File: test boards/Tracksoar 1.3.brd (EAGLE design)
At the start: 50.4 x 19.5 mm, 46 parts, among them IC1 BME280, IC2 74AHC1G125DBV, Y1 16MHZ

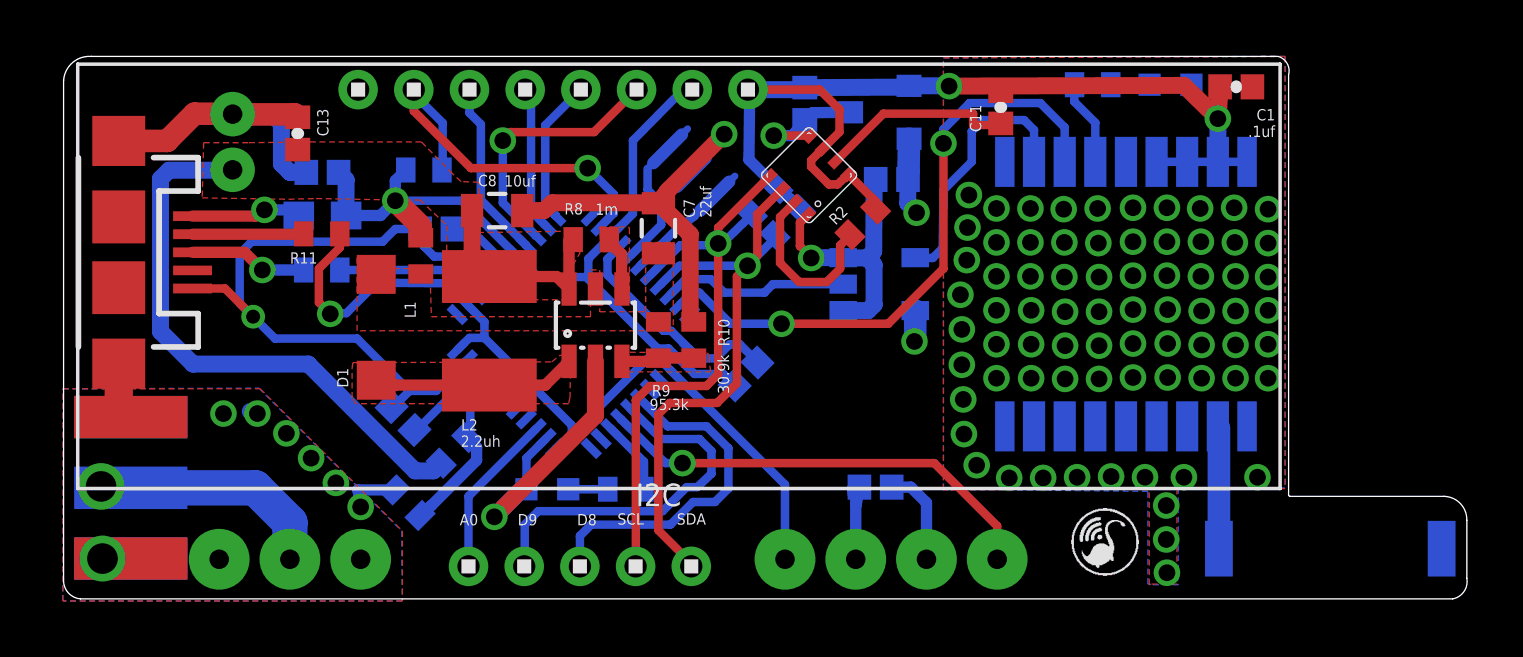
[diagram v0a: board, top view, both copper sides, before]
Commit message: Tracksoar V1.3
Created a new test board Tracksoar v1.3 to resolve potential issues
with the boost converter interfering with GPS reception.
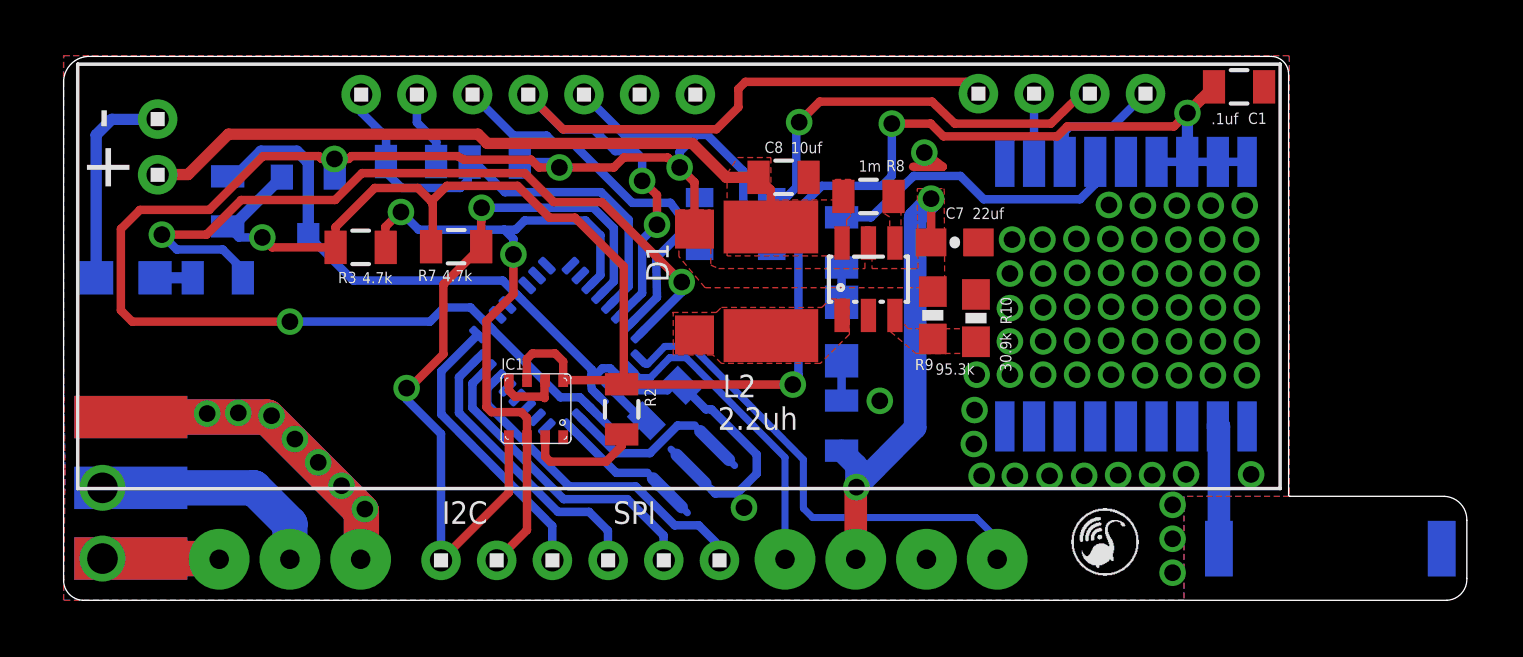
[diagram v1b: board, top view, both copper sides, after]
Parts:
- removed C10, C11, C13, C9: .1uf, SparkFun-Capacitors:0402-CAP
- removed C12: 1uf, SparkFun-Capacitors:0402-CAP
- removed C6: .1uf, SparkFun-Passives:0402-CAP
- removed F1: PTC0603, SparkFun-PowerIC:0603
- removed J1: (no value), SparkFun-Connectors:JST-2-PTH
- removed JP1: USB-MICROB, SparkFun-Connectors:USB-MICROB
- removed L1: BLM15HB121SN1, inductors:0402
- removed R11, R4: 22ohm, adafruit:R0402
- removed R13: 10k, adafruit:R0402
- removed U$4: ATMEGA32U4QFN2, SparkFun-DigitalIC:QFN-44-NOPAD
- added SERIAL: 1X4, headers(2mm):1X4
- added SPI/I2C: 1X6, headers(2mm):1X6
- added U1: ATMEGA328P, SparkFun-DigitalIC:MLF32
- C1, C2, C3, C4: device SparkFun-Capacitors:0402-CAP -> SparkFun-Capacitors:0805
- C5: value 1uf -> .1uf; device SparkFun-Capacitors:0402-CAP -> SparkFun-Capacitors:0805
- C7: device SparkFun-Capacitors:0805 -> SparkFun-Capacitors:0603-CAP
- FTDI: value 1X8 -> 1X7; device headers(2mm):1X8 -> headers(2mm):1X7
- GPSLOCK, PTT: device adafruit:CHIP-LED0603 -> adafruit:CHIP-LED0805
- R1, R2, R3, R5, R6, R7, R8: device adafruit:R0402 -> SparkFun-Resistors:0805
- R10, R9: device adafruit:R0402 -> SparkFun-Resistors:0603-RES
- U$3: value 1X5 -> 1X2; device headers(2mm):1X5 -> headers(2mm):1X2
- moved U$3 21.4 mm to (3.40, 16.3), turned to 90 degrees
- moved C2 21.0 mm to (5.92, 14.4), turned to 270 degrees
- moved LM3480 20.8 mm to (8.81, 14.2), turned to 180 degrees
- moved PTT 16.9 mm to (2.26, 11.6)
- moved R6 16.5 mm to (5.56, 11.6)
- moved R3 15.4 mm to (10.7, 12.7), flipped to the top, turned to 0 degrees
- moved GPSLOCK 14.8 mm to (28.0, 9.68), turned to 180 degrees
- moved IC1 12.9 mm to (17.0, 6.91), turned to 0 degrees
- moved D1 11.5 mm to (22.7, 11.5)
- moved C3 11.5 mm to (21.6, 7.11), turned to 315 degrees
- moved R7 11.2 mm to (14.1, 12.7), flipped to the top, turned to 0 degrees
- moved R2 11.0 mm to (20.1, 6.88), turned to 270 degrees
- moved Y1 10.7 mm to (22.6, 4.73), turned to 315 degrees
- moved C7 10.7 mm to (32.0, 12.9), turned to 0 degrees
- moved R1 10.6 mm to (28.0, 12.9), turned to 270 degrees
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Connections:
- removed net A0: U$3.1, U$4.36
- removed net D+: R4.2, U$4.4
- removed net D-: R11.2, U$4.3
- removed net D13: U$4.32
- removed net D8: U$3.3, U$4.28
- removed net D9: U$3.2, U$4.29
- removed net N$17: C12.2, U$4.42
- removed net N$19: C7.1, D1.C, L1.1, LT3426.5, R9.2
- removed net N$20: C5.2, U$4.6
- removed net N$7: JP1.D-, R11.1
- removed net N$8: JP1.D+, R4.1
- removed net RX: U$1.3_RXD1, U$4.21
- removed net VIN: C13.2, C8.1, J1.2, L2.1, LT3426.6, R13.1, R8.2
- removed net VSENSE: C6.2, R13.2, U$4.41
- removed net XTAL1: U$4.17, Y1.1
- removed net XTAL2: U$4.16, Y1.3
- new net 15V: C8.1, L2.1, LT3426.6, R8.2, U$3.1
- new net DTR: C5.1, FTDI.6
- new net N$26: U1.7, Y1.1
- new net RX1: SERIAL.1, U$1.3_RXD1
- new net RXO: FTDI.4, SERIAL.4, U1.30
- new net TXO: FTDI.5, IC2.2, U1.31
- net !RESET: now also C5.2, U1.29; no longer U$4.13
- net 3V: no longer C11.2, FTDI.1
- net D3: now also U1.1; no longer U$4.30
- net D4: now also U1.2; no longer U$4.25
- net GND: now also FTDI.1, FTDI.2, U$3.2, U1.21, U1.3, U1.5; no longer C10.1, C11.1, C12.1, C13.1, C5.1, C6.1, C9.1, FTDI.8, J1.1, JP1.GND, JP1.MT1, JP1.MT2, U$4.15, U$4.23, U$4.35, U$4.43, U$4.5
- net LED: now also U1.32; no longer U$4.31
- net MISO: now also SPI/I2C.4, U1.16; no longer FTDI.4, U$4.11
- net MOSI: now also SPI/I2C.5, U1.15; no longer FTDI.5, U$4.10
- net N$14: now also U1.8, Y1.3; no longer F1.1, JP1.VBUS
- net SCK: now also SPI/I2C.3, U1.17; no longer FTDI.3, U$4.9
- net SCL: now also SPI/I2C.1, U1.28; no longer U$3.4, U$4.18
- net SDA: now also SPI/I2C.2, U1.27; no longer U$3.5, U$4.19
- net SS: now also SPI/I2C.6, U1.14; no longer FTDI.6, U$4.8
- net TX: now also SERIAL.3, U$1.2_TXD1; no longer IC2.2, U$4.20
- net TX1: now also SERIAL.2; no longer U$1.2_TXD1
- net VCC: now also C7.1, D1.C, FTDI.3, LT3426.5, R9.2, U1.18, U1.4, U1.6; no longer C10.2, C9.2, F1.2, FTDI.2, L1.2, U$4.14, U$4.2, U$4.24, U$4.34, U$4.44, U$4.7
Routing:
- net VCC: track 51.9 -> 81.5 mm, vias 3 -> 6
- net RXO: track 0.00 -> 29.4 mm, vias 0 -> 2
- net VIN: track 28.0 -> 0.00 mm
- net 3V: track 39.9 -> 67.7 mm, vias 2 -> 4
- net GND: track 100.0 -> 72.5 mm, vias 85 -> 70
- net 15V: track 0.00 -> 24.8 mm
- net LED: track 2.67 -> 27.4 mm, vias 0 -> 2
- net RX: track 22.3 -> 0.00 mm, vias 2 -> 0
- net TXO: track 0.00 -> 14.7 mm
- net D9: track 13.3 -> 0.00 mm
- net D8: track 12.5 -> 0.00 mm
- net D-: track 9.34 -> 0.00 mm, vias 1 -> 0
- net PPS: track 3.08 -> 11.1 mm
- net N$9: track 7.30 -> 0.00 mm
- net VSENSE: track 6.19 -> 0.00 mm
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- added copper zone on layer 1, net 15V
- added copper zone on layer 1, net VCC
- removed copper zone on layer 2, net GND
- removed copper zone on layer 1, net N$19
- removed copper zone on layer 15, net VCC
- removed copper zone on layer 1, net VIN
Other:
- outline, holes or cut-outs redrawn
- board text added: "+"
- board text added: "-"
- board text added: "FTDI"
- board text added: "Tracksoar v1.2"
- board text removed: "!RESET"
- board text removed: "3V"
- board text removed: "5V"
- board text removed: "74AHC1G125"
- board text removed: "A0"
- board text removed: "D8"
- board text removed: "D9"
- board text removed: "MISO"
- board text removed: "MOSI"
- board text removed: "SCK"
- board text removed: "SCL"
- board text removed: "SDA"
- board text removed: "SS"
- board text removed: "Tracksoar v2"
